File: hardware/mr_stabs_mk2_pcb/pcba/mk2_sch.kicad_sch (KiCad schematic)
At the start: 69 parts, among them U1 INA228, U2 TPS54202DDC, U3 AP2112K-3.3, U4 BNO055, U5 USBLC6-2SC6, Y1 32.768kHz

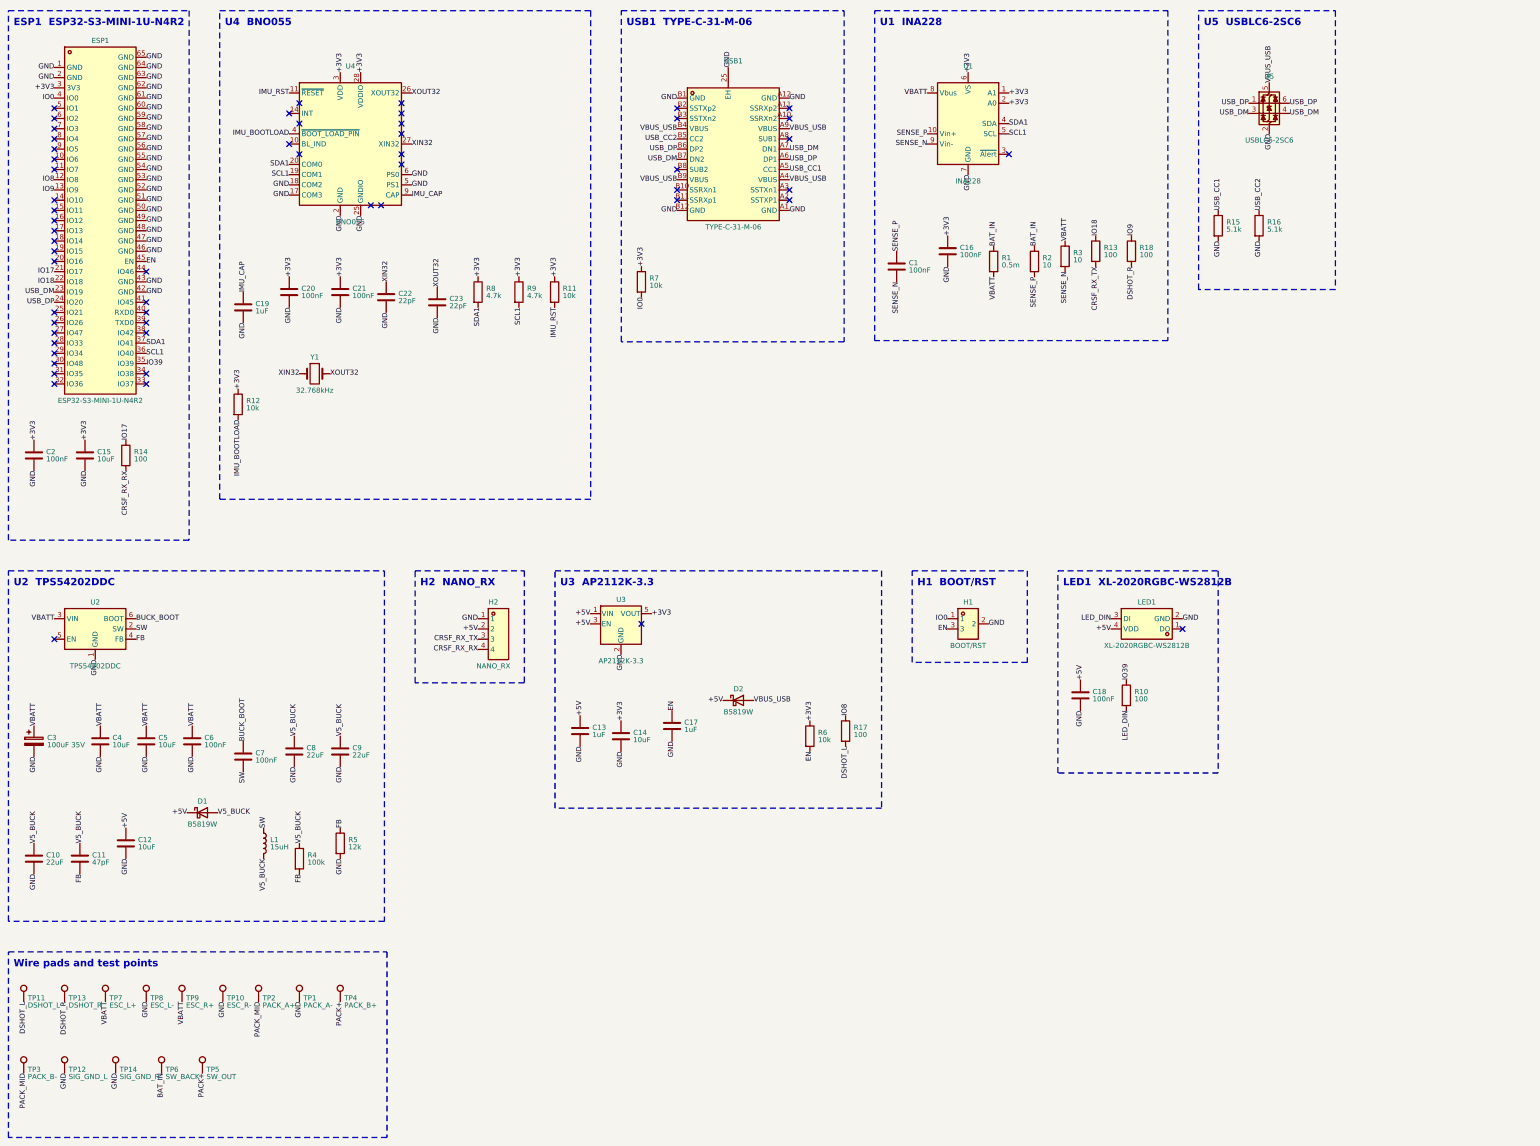
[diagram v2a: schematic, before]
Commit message: Move the Mk2 USB-C and bulk cap into the stem; swap to INA238 and TYPE-C-31-D-06
- USB-C and the 100 uF bulk cap sit in the stem between the bosses, away from the motors under
  the ears. BOOT/RST moved to the left ear, the BNO055 block front-right of the USB-C's shell
  legs; two caps went to the wedge face under the parts they serve (no GND via room on top);
  two fixed GND stitching vias keep the stem's bottom pour joined.
- JLCPCB assembly had no INA228 and flagged the 24-pin USB-C as hard to source: INA238
  (C2868250, same pinout, 16-bit) and HRO TYPE-C-31-D-06 (C2689964, 16-pin USB 2.0), both
  reviewed against their datasheets. Paste in the USB-C's shell slots so reflow solders them.
- Re-routed: 0 errors, 0 unconnected. Order files (ORDER.md: PCBA Qty 2), STEP, schematic and
  simulations regenerated.

Firmware: the INA238 needs device ID 0x238, 16-bit reads, ADCRANGE 1 and SHUNT_OHMS 0.0005.

Co-Authored-By: Claude Opus 5.5 <noreply@anthropic.com>
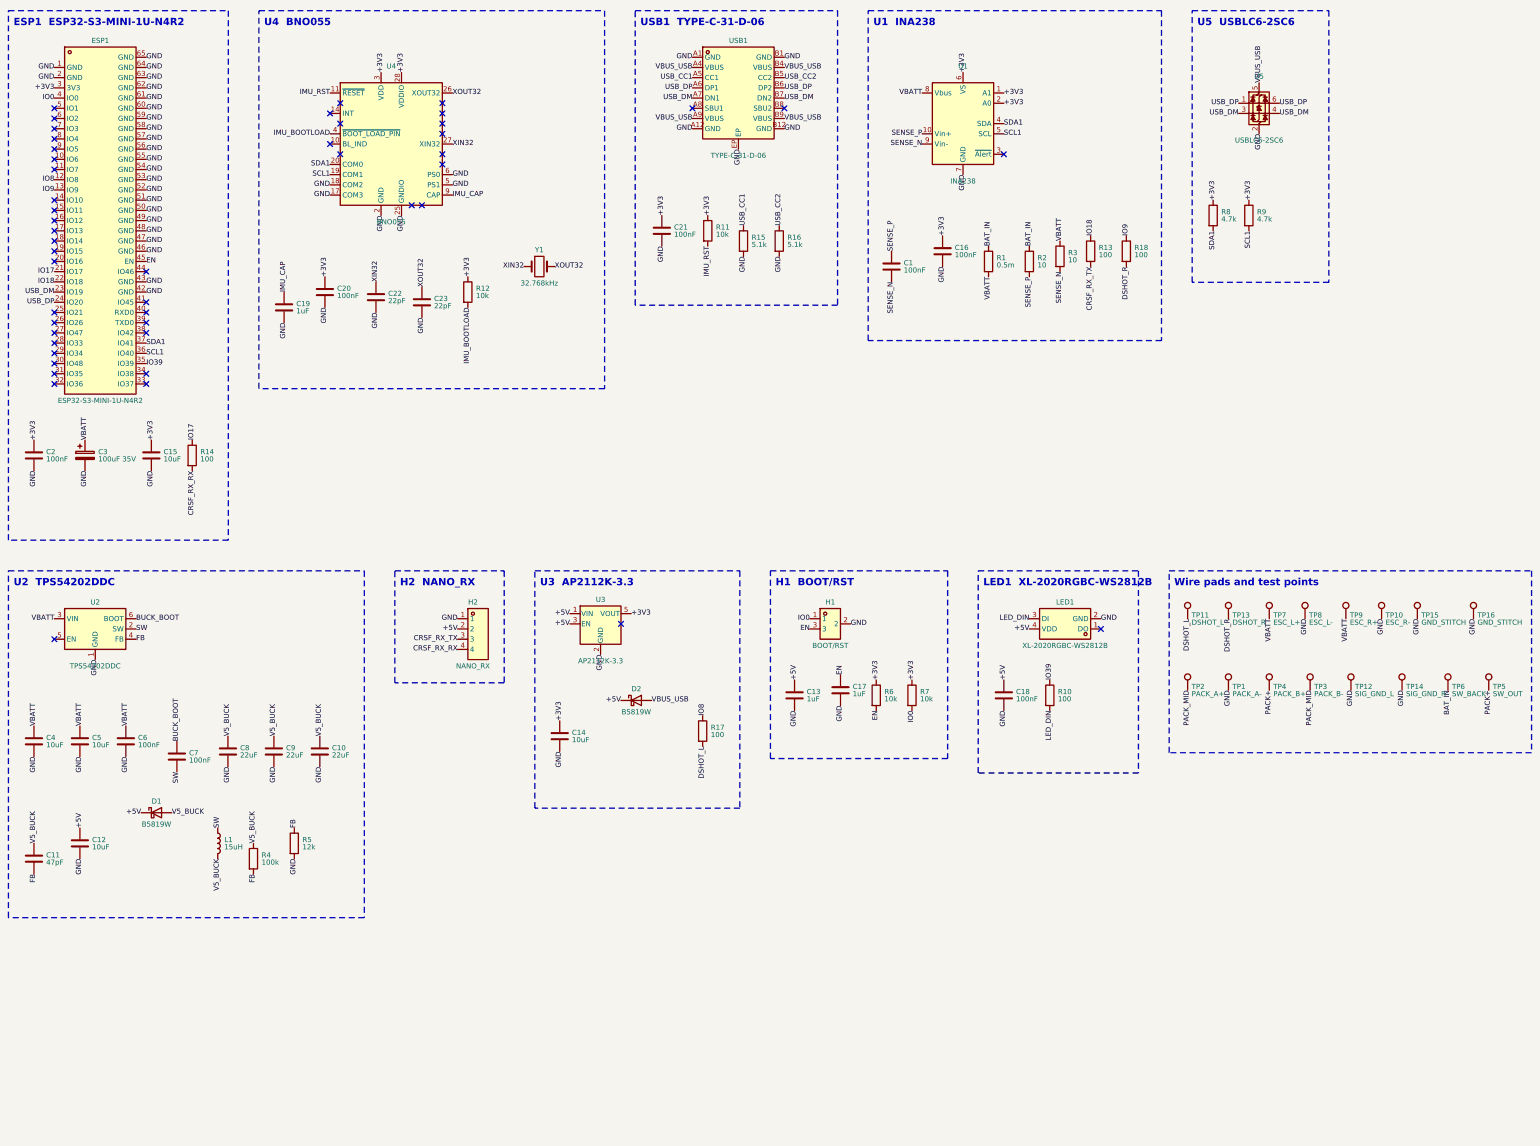
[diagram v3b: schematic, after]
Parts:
- removed C1, C16: 100nF, symbol Device:C
- removed C14: 10uF, symbol Device:C
- removed D2: B5819W, symbol Device:D_Schottky
- removed R12: 10k, symbol Device:R
- removed R17: 100, symbol Device:R
- removed TP12: SIG_GND_L, symbol Connector:TestPoint
- removed TP14: SIG_GND_R, symbol Connector:TestPoint
- removed TP3: PACK_B-, symbol Connector:TestPoint
- removed TP5: SW_OUT, symbol Connector:TestPoint
- removed TP6: SW_BACK, symbol Connector:TestPoint
- removed U3: AP2112K-3.3, symbol Regulator_Linear:AP2112K-3.3
- removed U4: BNO055, symbol Sensor_Motion:BNO055
- removed USB1: TYPE-C-31-M-06, symbol mk2:TYPE-C-31-M-06
- removed Y1: 32.768kHz, symbol Device:Crystal
- added C18, C2, C21: 100nF, symbol Device:C
- added C19: 1uF, symbol Device:C
- added D1: B5819W, symbol Device:D_Schottky
- added H2: NANO_RX, symbol mk2:HXPZ2.54-1X4PWT
- added R4: 100k, symbol Device:R
- added R5: 12k, symbol Device:R
- added R7: 10k, symbol Device:R
- added R8: 4.7k, symbol Device:R
- added TP10: ESC_R-, symbol Connector:TestPoint
- added TP11: DSHOT_L, symbol Connector:TestPoint
- added TP13: DSHOT_R, symbol Connector:TestPoint
- added TP15: GND_STITCH, symbol Connector:TestPoint
- added TP7: ESC_L+, symbol Connector:TestPoint
- added TP8: ESC_L-, symbol Connector:TestPoint
- added U1: INA238, symbol Sensor_Energy:INA238
- C1: renamed from R7; value 10k -> 100nF; symbol Device:R -> Device:C
- C14: renamed from R4; value 100k -> 10uF; symbol Device:R -> Device:C
- C15: renamed from C2; value 100nF -> 10uF
- C16: renamed from U1; value INA228 -> 100nF; symbol Sensor_Energy:INA228 -> Device:C
- C20: renamed from C19; value 1uF -> 100nF
- C22: renamed from C20; value 100nF -> 22pF
- C23: renamed from C21; value 100nF -> 22pF
- D2: renamed from R5; value 12k -> B5819W; symbol Device:R -> Device:D_Schottky
- R12: renamed from C22; value 22pF -> 10k; symbol Device:C -> Device:R
- R14: renamed from C15; value 10uF -> 100; symbol Device:C -> Device:R
- R17: renamed from H2; value NANO_RX -> 100; symbol mk2:HXPZ2.54-1X4PWT -> Device:R
- TP1: renamed from TP7; value ESC_L+ -> PACK_A-
- TP12: renamed from TP10; value ESC_R- -> SIG_GND_L
- TP14: renamed from TP2; value PACK_A+ -> SIG_GND_R
- TP16: renamed from TP11; value DSHOT_L -> GND_STITCH
- TP2: renamed from TP13; value DSHOT_R -> PACK_A+
- TP3: renamed from TP9; value ESC_R+ -> PACK_B-
- TP4: renamed from TP8; value ESC_L- -> PACK_B+
- TP5: renamed from TP4; value PACK_B+ -> SW_OUT
- TP6: renamed from TP1; value PACK_A- -> SW_BACK
- TP9: renamed from C18; value 100nF -> ESC_R+; symbol Device:C -> Connector:TestPoint
- U3: renamed from D1; value B5819W -> AP2112K-3.3; symbol Device:D_Schottky -> Regulator_Linear:AP2112K-3.3
- U4: renamed from R14; value 100 -> BNO055; symbol Device:R -> Sensor_Motion:BNO055
- USB1: renamed from R8; value 4.7k -> TYPE-C-31-D-06; symbol Device:R -> mk2:TYPE-C-31-D-06
- Y1: renamed from C23; value 22pF -> 32.768kHz; symbol Device:C -> Device:Crystal
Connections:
- net +3V3: now also C14.1, C20.1, R12.1, U3.5 (VOUT), U4.28 (VDDIO), U4.3 (VDD), C2.1, C21.1, R7.1, R8.1, U1.1 (A1), U1.2 (A0), U1.6 (VS); no longer C1.1, C16.2 (A0), C16.6 (VS), C22.1, C23.1, R14.1, USB1.1
- net +5V: now also D2.1 (K), U3.3 (EN), C18.1, D1.1 (K), H2.2; no longer R17.2, TP9.1
- net BAT_IN: now also TP6.1
- net CRSF_RX_RX: now also R14.2, H2.4; no longer R17.4, U4.2
- net CRSF_RX_TX: now also H2.3; no longer R17.3
- net DSHOT_L: now also R17.2, TP11.1; no longer TP16.1
- net DSHOT_R: now also TP13.1; no longer TP2.1
- net FB: now also R4.2, R5.1; no longer C14.2, D2.1
- net GND: now also C14.2, C16.2, TP1.1, TP14.1, TP16.1, U3.2 (GND), U4.17 (COM3), U4.18 (COM2), U4.2 (GND), U4.25 (GNDIO), U4.5 (PS1), U4.6 (PS0), USB1.A1 (GND), USB1.A12 (GND), USB1.B1 (GND), USB1.B12 (GND), USB1.EP, C18.2, C19.2, C2.2, C21.2, H2.1, R5.2, TP10.1, TP15.1, TP8.1, U1.7 (GND); no longer C16.7 (GND), D2.2, R12.2, R14.2, R17.1, TP4.1, TP6.1, TP9.2, Y1.2
- net IMU_BOOTLOAD: now also R12.2, U4.4 (~{BOOT_LOAD_PIN})
- net IMU_CAP: now also U4.9 (CAP), C19.1; no longer C20.1
- net IMU_RST: now also U4.11 (~{RESET})
- net IO0: now also R7.2; no longer C1.2
- net IO17: now also R14.1; no longer U4.1
- net IO8: now also R17.1
- net PACK+: now also TP4.1
- net PACK_MID: now also TP2.1, TP3.1; no longer TP14.1
- net SCL1: now also U4.19 (COM1), U1.5 (SCL); no longer C16.5 (SCL)
- net SDA1: now also U4.20 (COM0), R8.2, U1.4 (SDA); no longer C16.4 (SDA), USB1.2
- net SENSE_N: now also C1.2, U1.9 (Vin-); no longer C16.9 (Vin-)
- net SENSE_P: now also C1.1, U1.10 (Vin+); no longer C16.10 (Vin+)
- net USB_CC1: now also USB1.A5 (CC1)
- net USB_CC2: now also USB1.B5 (CC2)
- net USB_DM: now also USB1.A7 (DN1), USB1.B7 (DN2)
- net USB_DP: now also USB1.A6 (DP1), USB1.B6 (DP2)
- net V5_BUCK: now also D1.2 (A), R4.1; no longer C14.1, U3.2 (A)
- net VBATT: now also TP9.1, TP7.1, U1.8 (Vbus); no longer C16.8 (Vbus), TP1.1, TP3.1
- net VBUS_USB: now also D2.2 (A), USB1.A4 (VBUS), USB1.A9 (VBUS), USB1.B4 (VBUS), USB1.B9 (VBUS)
- net XIN32: now also C22.1, U4.27 (XIN32), Y1.1; no longer R12.1
- net XOUT32: now also C23.1, U4.26 (XOUT32), Y1.2; no longer Y1.1
- no-connect marks 56 -> 48
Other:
- note added: "U1 INA238"
- note added: "USB1 TYPE-C-31-D-06"
- note removed: "U1 INA228"
- note removed: "USB1 TYPE-C-31-M-06"
- moved on the sheet: C15, C20, C22, C23, TP1, TP12, TP14, TP16, TP2, TP3, TP4, TP5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

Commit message: Mk2 board v1.0: inner planes in the gerbers, signature, rounded corners, wired schematic
- gerbers.zip now has In1 and In2. fab.sh exported only F.Cu and B.Cu, so every earlier zip
  for this 4-layer board was missing both GND planes. ORDER.md says to check for 4 copper
  files.
- Silkscreen: "MR STABS MK2" and "v1.0 BEN W 2026" replace the XT60 pad legend on the bottom
  left ear (the roof-face pads keep their own labels), with the BWBots logo above them.
  VERSION in silk.py sets the revision.
- Convex outline corners filleted to 1 mm (corner_radius in gen_placement.py). Placement and
  routing unchanged; zones refilled. DRC 0 errors, 0 unconnected.
- Schematic redrawn as three hierarchical sheets (power, MCU and USB, IMU and radio) with
  nets as wires; connectivity matches mk2.net on all 37 nets.
- STEP, BOM, CPL and renders regenerated from the same board.

Co-Authored-By: Claude Opus 5.5 <noreply@anthropic.com>
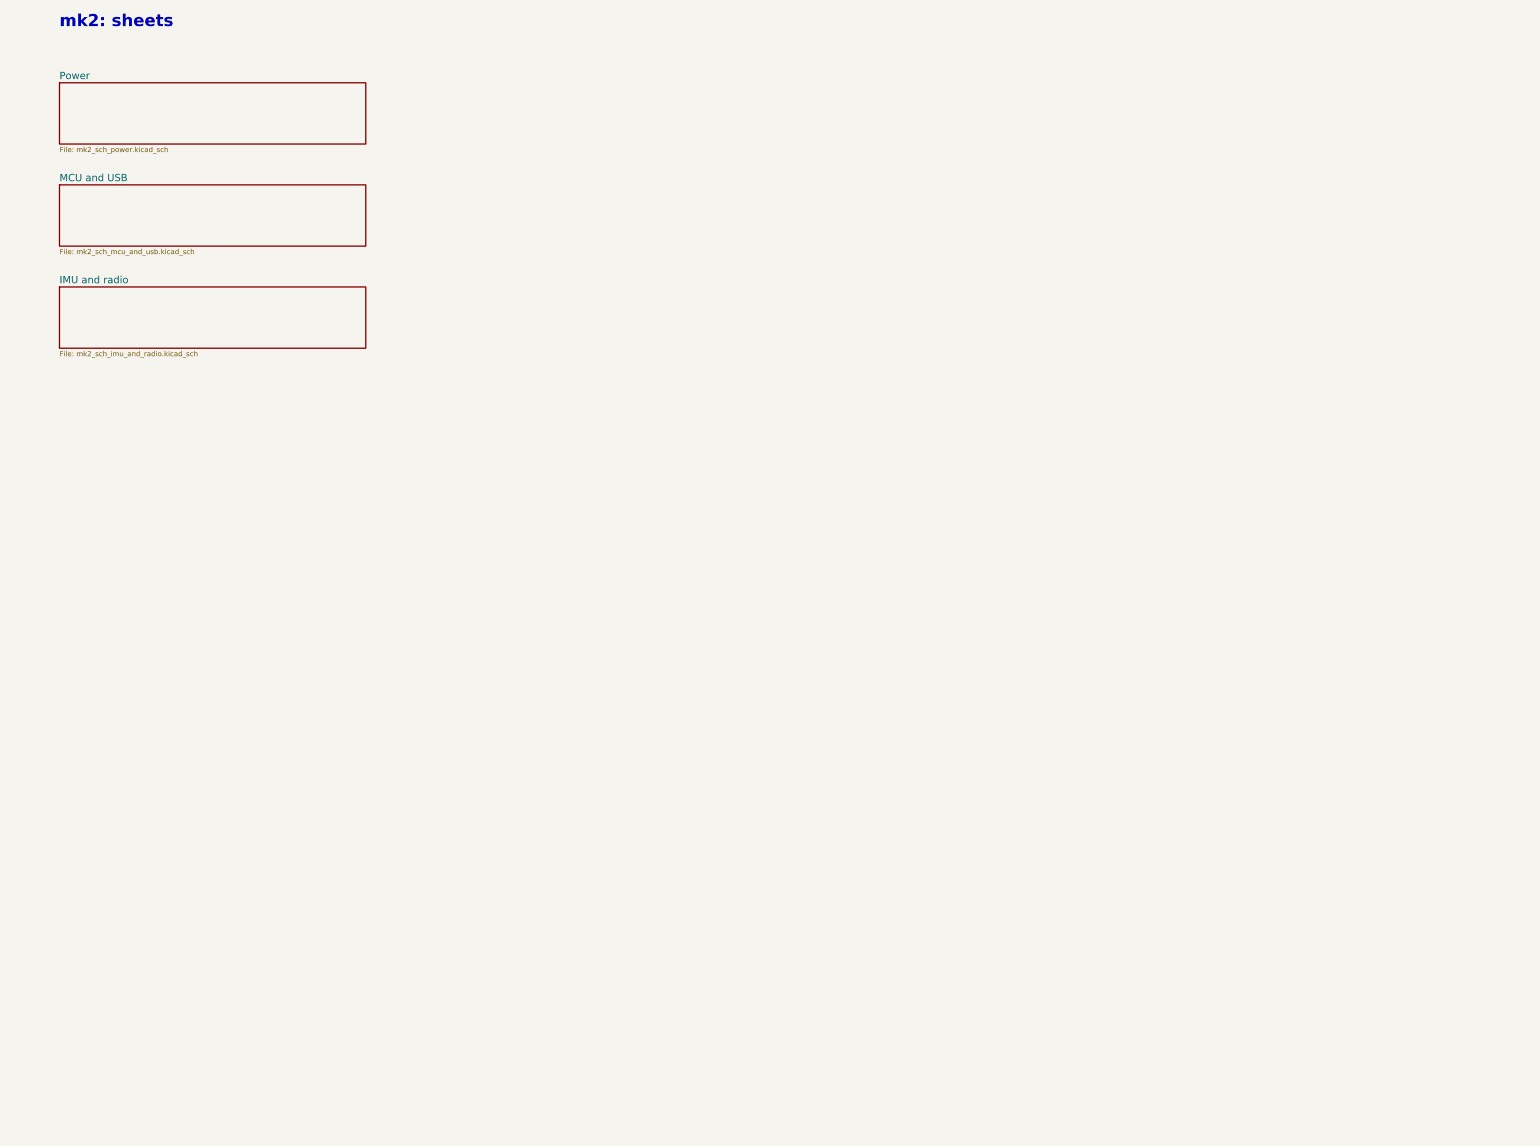
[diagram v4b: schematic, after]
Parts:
- removed C1, C16, C18, C2, C20, C21, C6, C7: 100nF, symbol Device:C
- removed C10, C8, C9: 22uF, symbol Device:C
- removed C11: 47pF, symbol Device:C
- removed C12, C14, C15, C4, C5: 10uF, symbol Device:C
- removed C13, C17, C19: 1uF, symbol Device:C
- removed C22, C23: 22pF, symbol Device:C
- removed C3: 100uF 35V, symbol Device:C_Polarized
- removed D1, D2: B5819W, symbol Device:D_Schottky
- removed ESP1: ESP32-S3-MINI-1U-N4R2, symbol mk2:ESP32-S3-MINI-1U-N4R2
- removed H1: BOOT/RST, symbol mk2:HXPZ2.54-1X3PTP-YQ
- removed H2: NANO_RX, symbol mk2:HXPZ2.54-1X4PWT
- removed L1: 15uH, symbol Device:L
- removed LED1: XL-2020RGBC-WS2812B, symbol mk2:XL-2020RGBC-WS2812B
- removed R1: 0.5m, symbol Device:R
- removed R10, R13, R14, R17, R18: 100, symbol Device:R
- removed R11, R12, R6, R7: 10k, symbol Device:R
- removed R15, R16: 5.1k, symbol Device:R
- removed R2, R3: 10, symbol Device:R
- removed R4: 100k, symbol Device:R
- removed R5: 12k, symbol Device:R
- removed R8, R9: 4.7k, symbol Device:R
- removed TP1: PACK_A-, symbol Connector:TestPoint
- removed TP10: ESC_R-, symbol Connector:TestPoint
- removed TP11: DSHOT_L, symbol Connector:TestPoint
- removed TP12: SIG_GND_L, symbol Connector:TestPoint
- removed TP13: DSHOT_R, symbol Connector:TestPoint
- removed TP14: SIG_GND_R, symbol Connector:TestPoint
- removed TP15, TP16: GND_STITCH, symbol Connector:TestPoint
- removed TP2: PACK_A+, symbol Connector:TestPoint
- removed TP3: PACK_B-, symbol Connector:TestPoint
- removed TP4: PACK_B+, symbol Connector:TestPoint
- removed TP5: SW_OUT, symbol Connector:TestPoint
- removed TP6: SW_BACK, symbol Connector:TestPoint
- removed TP7: ESC_L+, symbol Connector:TestPoint
- removed TP8: ESC_L-, symbol Connector:TestPoint
- removed TP9: ESC_R+, symbol Connector:TestPoint
- removed U1: INA238, symbol Sensor_Energy:INA238
- removed U2: TPS54202DDC, symbol Regulator_Switching:TPS54202DDC
- removed U3: AP2112K-3.3, symbol Regulator_Linear:AP2112K-3.3
- removed U4: BNO055, symbol Sensor_Motion:BNO055
- removed U5: USBLC6-2SC6, symbol Power_Protection:USBLC6-2SC6
- removed USB1: TYPE-C-31-D-06, symbol mk2:TYPE-C-31-D-06
- removed Y1: 32.768kHz, symbol Device:Crystal
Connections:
- no-connect marks 48 -> 0
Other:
- added sheet IMU and radio (mk2_sch_imu_and_radio.kicad_sch)
- added sheet MCU and USB (mk2_sch_mcu_and_usb.kicad_sch)
- added sheet Power (mk2_sch_power.kicad_sch)
- note added: "mk2: sheets"
- note removed: "ESP1 ESP32-S3-MINI-1U-N4R2"
- note removed: "H1 BOOT/RST"
- note removed: "H2 NANO_RX"
- note removed: "LED1 XL-2020RGBC-WS2812B"
- note removed: "U1 INA238"
- note removed: "U2 TPS54202DDC"
- note removed: "U3 AP2112K-3.3"
- note removed: "U4 BNO055"
- note removed: "U5 USBLC6-2SC6"
- note removed: "USB1 TYPE-C-31-D-06"
- note removed: "Wire pads and test points"
